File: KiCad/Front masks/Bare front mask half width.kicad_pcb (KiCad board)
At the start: 2 copper layers, 17.2 x 111.5 mm, 3 parts

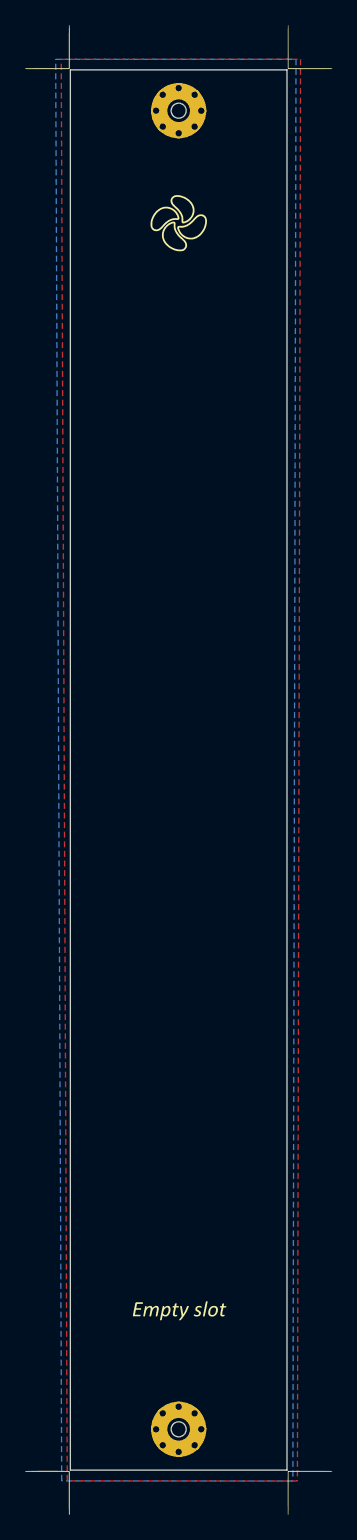
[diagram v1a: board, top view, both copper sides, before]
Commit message: Bare front masks resized
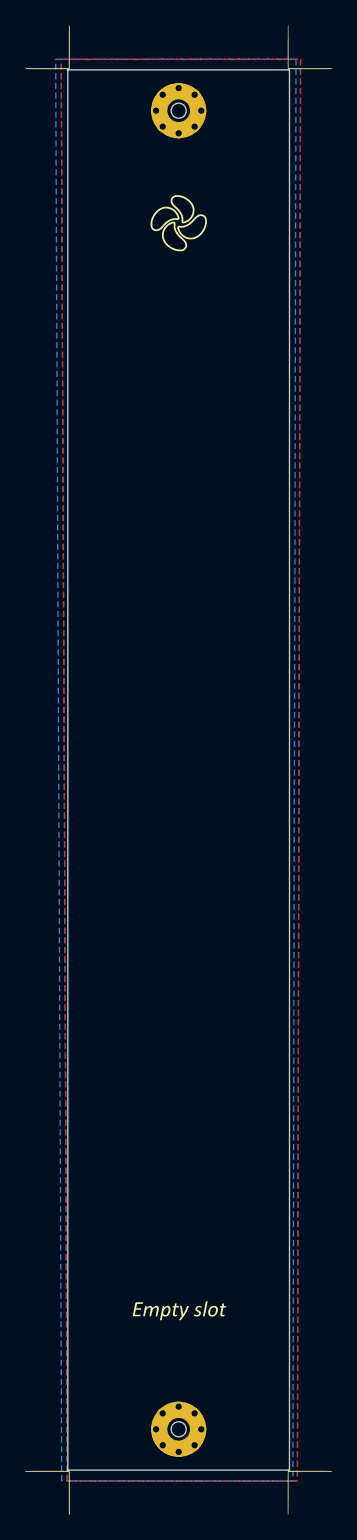
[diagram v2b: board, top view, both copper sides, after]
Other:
- board size 17.2 x 111.5 mm -> 17.6 x 111.5 mm
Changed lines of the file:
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@@
 			(layer "F.SilkS"
 				(type "Top Silk Screen")
+				(color "Black")
 			)
 			(layer "F.Paste"
@@
 			(layer "F.Mask"
 				(type "Top Solder Mask")
+				(color "White")
 				(thickness 0.01)
 			)
@@
 			(layer "dielectric 1"
 				(type "core")
+				(color "FR4 natural")
 				(thickness 1.51)
 				(material "FR4")
@@
 			(layer "B.Mask"
 				(type "Bottom Solder Mask")
+				(color "White")
 				(thickness 0.01)
 			)
@@
 			(layer "B.SilkS"
 				(type "Bottom Silk Screen")
+				(color "Black")
 			)
 			(copper_finish "None")
@@
 		(capping no)
 		(filling no)
+		(zone_defaults)
 		(aux_axis_origin 140.5 150)
 		(grid_origin 140.5 150)
 		(pcbplotparams
-			(layerselection 0x00000000_00000000_55555555_57555557)
+			(layerselection 0x00000000_00000000_55555555_5755f57f)
 			(plot_on_all_layers_selection 0x00000000_00000000_00000000_00000000)
 			(disableapertmacros no)
@@
 	)
 	(gr_rect
-		(start 140.4 144.6)
-		(end 175.5 150.1)
+		(start 140.3 38.5)
+		(end 157.95 44)
 		(stroke
 			(width 0.1)
@@
 	)
 	(gr_rect
-		(start 140.5 38.5)
-		(end 175.4 44)
+		(start 140.4 144.6)
+		(end 157.95 150.1)
 		(stroke
 			(width 0.1)
@@
 	)
 	(gr_rect
-		(start 140.5 144.6)
-		(end 175.4 150)
+		(start 140.3 38.5)
+		(end 157.95 44)
 		(stroke
 			(width 0.1)
@@
 		)
 		(fill yes)
-		(layer "F.Paste")
+		(layer "B.Mask")
 	)
 	(gr_rect
-		(start 140.52 38.5)
-		(end 175.42 44)
+		(start 140.354616 144.55)
+		(end 157.904616 150.05)
 		(stroke
 			(width 0.1)
@@
 		)
 		(fill yes)
-		(layer "F.Paste")
+		(layer "B.Mask")
 	)
 	(gr_rect
-		(start 190.17 144.83)
-		(end 207.62 150.33)
+		(start 140.3 38.5)
+		(end 158 44)
 		(stroke
 			(width 0.1)
@@
 	)
 	(gr_rect
-		(start 190.19 38.73)
-		(end 207.64 44.23)
+		(start 140.3 144.6)
+		(end 157.959232 150)
 		(stroke
 			(width 0.1)
@@
 		(layer "F.Paste")
 	)
-	(gr_line
-		(start 140.5 150)
-		(end 140.5 38.5)
+	(gr_rect
+		(start 140.3 144.6)
+		(end 157.959232 150)
+		(stroke
+			(width 0.1)
+			(type solid)
+		)
+		(fill yes)
+		(layer "B.Paste")
+	)
+	(gr_rect
+		(start 140.425 38.5)
+		(end 157.875 44)
+		(stroke
+			(width 0.1)
+			(type solid)
+		)
+		(fill yes)
+		(layer "B.Paste")
+	)
+	(gr_rect
+		(start 140.3 38.5)
+		(end 157.95 150)
 		(stroke
 			(width 0.05)
-			(type solid)
-		)
-		(locked yes)
+			(type default)
+		)
+		(fill no)
 		(layer "Edge.Cuts")
 	)
@@
 		)
 		(fill no)
-		(layer "Edge.Cuts")
-	)
-	(gr_line
-		(start 157.75 38.5)
-		(end 140.5 38.5)
-		(stroke
-			(width 0.05)
-			(type solid)
-		)
-		(locked yes)
-		(layer "Edge.Cuts")
-	)
-	(gr_line
-		(start 157.75 38.5)
-		(end 157.75 150)
-		(stroke
-			(width 0.05)
-			(type solid)
-		)
-		(locked yes)
-		(layer "Edge.Cuts")
-	)
-	(gr_line
-		(start 157.75 150)
-		(end 140.5 150)
-		(stroke
-			(width 0.05)
-			(type solid)
-		)
-		(locked yes)
 		(layer "Edge.Cuts")
 	)
@@
 		(layer "User.1")
 		(pts
-			(xy 140.5 150) (xy 157.75 149.325)
+			(xy 140.3 150) (xy 157.95 149.325)
 		)
 		(height 2.4)
@@
 			(keep_text_aligned yes)
 		)
-		(gr_text "17,25 mm"
+		(gr_text "17,65 mm"
 			(at 149.125 151.25 0)
 			(layer "User.1")
@@
 	)
 	(zone
-		(layer "F.Cu")
+		(layers "F.Cu" "B.Cu")
+		(hatch edge 0.2)
+		(connect_pads no
+			(clearance 0.1)
+		)
+		(min_thickness 0.1)
+		(fill yes
+			(thermal_gap 0.5)
+			(thermal_bridge_width 0.5)
+			(island_removal_mode 1)
+		)
+		(polygon
+			(pts
+				(xy 139.772543 37.659812) (xy 158.829334 37.654701) (xy 158.579365 150.870423) (xy 140.252545 150.860387)
+			)
+		)
+	)
+	(zone
+		(layer "B.Cu")
 		(hatch edge 0.2)
 		(connect_pads
@@
 		(polygon
 			(pts
-				(xy 139.772543 37.659812) (xy 158.829334 37.654701) (xy 158.579365 150.870423) (xy 140.252545 150.860387)
-			)
-		)
-	)
-	(zone
-		(layer "B.Cu")
-		(hatch edge 0.2)
-		(connect_pads
-			(clearance 0.2)
-		)
-		(min_thickness 0.25)
-		(fill yes
-			(thermal_gap 0.5)
-			(thermal_bridge_width 0.5)
-			(island_removal_mode 1)
-		)
-		(polygon
-			(pts
 				(xy 139.330895 37.659318) (xy 158.468393 37.654179) (xy 158.218427 150.869399) (xy 139.810895 150.859318)
 			)
 		)
 	)
-	(group ""
-		(locked yes)
-		(members "02bb31b4-0d84-4d7d-b2de-8e9ac60e355a" "04a62722-e57a-4ba0-b164-c94581b168bb"
-			"cc5d43c5-6e42-4df4-862c-ebac80ed1cfe" "fdb9104b-7eb1-4899-8808-f9ade4fe7c0f"
-		)
-	)
